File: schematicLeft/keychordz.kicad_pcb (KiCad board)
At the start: 2 copper layers, 124 x 101 mm, 45 parts, among them IC1 MCP73833-BZI_UN, J1 USB_C_Receptacle_USB2.0, J2 Conn_01x04_Male, J3 Conn_01x04_Male, SW1 SW_Push, SW2 SW_Push, SW3 SW_Push, SW4 SW_Push, SW5 SW_Push, SW6 SW_Push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

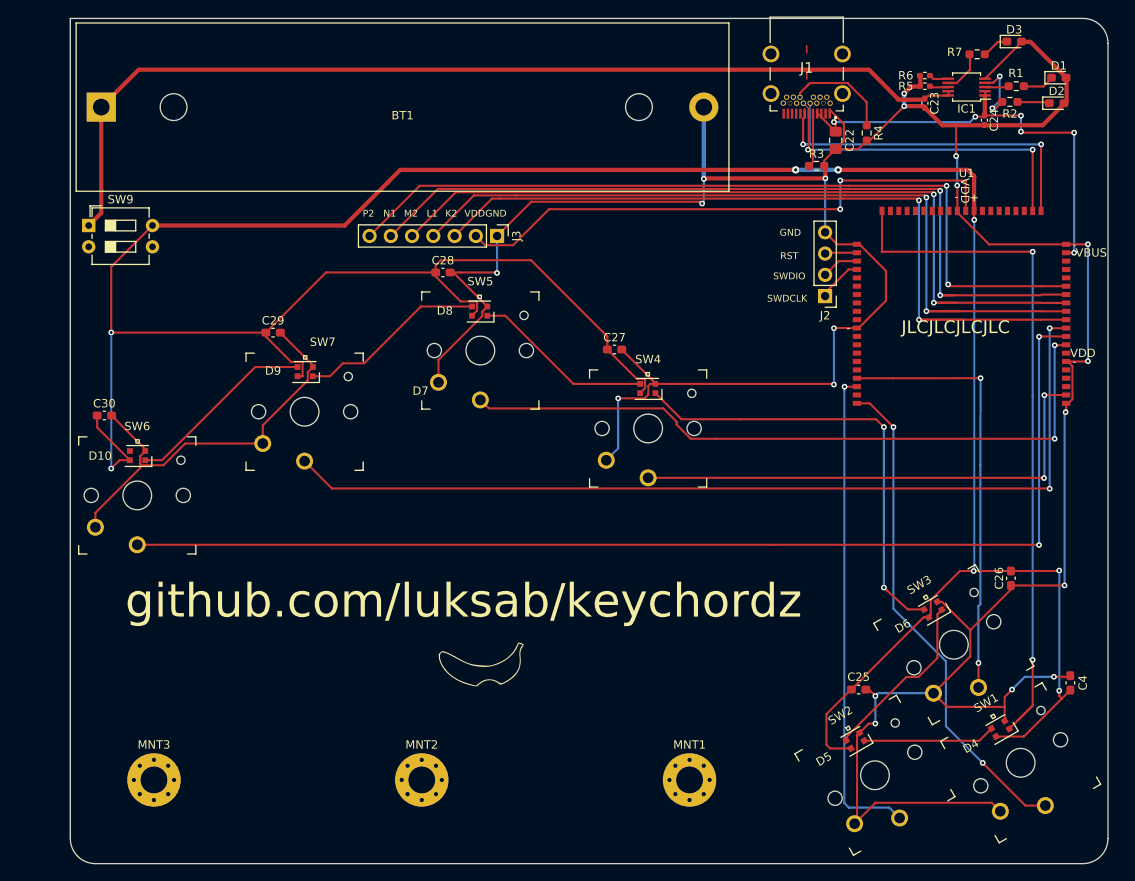
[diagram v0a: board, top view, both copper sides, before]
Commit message: change left PCB to STM32
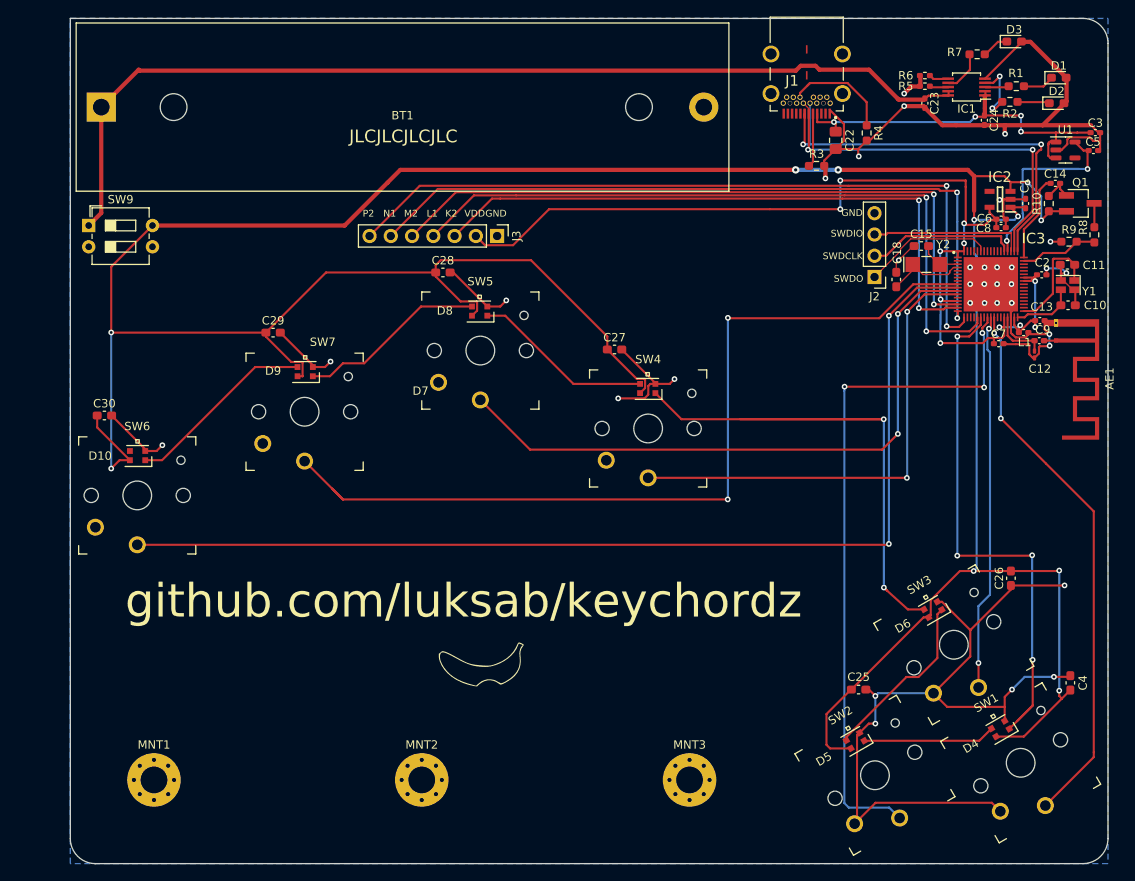
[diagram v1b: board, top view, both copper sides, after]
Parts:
- added AE1: PCB, RF_Antenna:Texas_SWRA117D_2.4GHz_Right, F.Cu at (129.8, 50.5)
- added C1: 1µF, Capacitor_SMD:C_0402_1005Metric_Pad0.74x0.62mm_HandSolder, F.Cu at (126.2, 34.1)
- added C10: 12pF, Capacitor_SMD:C_0603_1608Metric_Pad1.08x0.95mm_HandSolder, F.Cu at (131.2, 46.3)
- added C11: 12pF, Capacitor_SMD:C_0603_1608Metric_Pad1.08x0.95mm_HandSolder, F.Cu at (131.2, 41.4)
- added C12: 0.8pF, Capacitor_SMD:C_0201_0603Metric_Pad0.64x0.40mm_HandSolder, F.Cu at (127.2, 52.2)
- added C13: 1µF, Capacitor_SMD:C_0402_1005Metric_Pad0.74x0.62mm_HandSolder, F.Cu at (127.9, 48.1)
- added C14: 0.1µF, Capacitor_SMD:C_0402_1005Metric_Pad0.74x0.62mm_HandSolder, F.Cu at (129.7, 31.7)
- added C15: 12pF, Capacitor_SMD:C_0603_1608Metric_Pad1.08x0.95mm_HandSolder, F.Cu at (113.7, 39.2)
- added C18: 12pF, Capacitor_SMD:C_0603_1608Metric_Pad1.08x0.95mm_HandSolder, F.Cu at (110.7, 43.2)
- added C2: 1µF, Capacitor_SMD:C_0402_1005Metric_Pad0.74x0.62mm_HandSolder, F.Cu at (128.1, 42.6)
- added C3: 1µF, Capacitor_SMD:C_0402_1005Metric_Pad0.74x0.62mm_HandSolder, F.Cu at (134.5, 25.6)
- added C5: 1µF, Capacitor_SMD:C_0402_1005Metric_Pad0.74x0.62mm_HandSolder, F.Cu at (134.3, 27.8)
- added C6: 10µF, Capacitor_SMD:C_0402_1005Metric_Pad0.74x0.62mm_HandSolder, F.Cu at (123.2, 36.0)
- added C7: 1µF, Capacitor_SMD:C_0402_1005Metric_Pad0.74x0.62mm_HandSolder, F.Cu at (122.9, 50.9)
- added C8: 0.1µF, Capacitor_SMD:C_0402_1005Metric_Pad0.74x0.62mm_HandSolder, F.Cu at (123.2, 37.0)
- added C9: 100pF, Capacitor_SMD:C_0402_1005Metric_Pad0.74x0.62mm_HandSolder, F.Cu at (125.9, 49.5)
- added IC2: TPS7A2024PDBVR, SamacSys_Parts:SOT95P280X145-5N, F.Cu at (123.1, 33.6)
- added IC3: STM32WB55RGV7, SamacSys_Parts:QFN40P800X800X100-69N-D, F.Cu at (122.0, 43.8)
- added L1: 3.9nH, Inductor_SMD:L_0402_1005Metric_Pad0.77x0.64mm_HandSolder, F.Cu at (127.8, 50.5)
- added Q1: Q_PMOS_GSD, Package_TO_SOT_SMD:SC-59_Handsoldering, F.Cu at (132.7, 34.1)
- added R10: 10k, Resistor_SMD:R_0603_1608Metric_Pad0.98x0.95mm_HandSolder, F.Cu at (128.9, 34.1)
- added R8: 1k, Resistor_SMD:R_0603_1608Metric_Pad0.98x0.95mm_HandSolder, F.Cu at (134.4, 37.9)
- added R9: 1k, Resistor_SMD:R_0603_1608Metric_Pad0.98x0.95mm_HandSolder, F.Cu at (131.3, 38.7)
- added Y1: Crystal_GND23, Crystal:Crystal_SMD_2016-4Pin_2.0x1.6mm_HandSoldering, F.Cu at (131.2, 43.9)
- added Y2: Crystal, Crystal:Crystal_SMD_MicroCrystal_CC7V-T1A-2Pin_3.2x1.5mm_HandSoldering, F.Cu at (114.3, 41.4)
- J2: value Conn_01x04_Male -> DEBUG_CONN
- J3: value Conn_01x04_Male -> OLED_CONN
- U1: value nRF52840_Breakout -> MIC5504-3.3YM5; footprint schematic:nRF52840_Breakout -> Package_TO_SOT_SMD:SOT-23-5
- moved MNT1 64.0 mm to (22.0, 103.0)
- moved MNT3 64.0 mm to (86.0, 103.0)
- moved U1 14.0 mm to (130.9, 27.7)
- moved J2 6.33 mm to (108.1, 42.9)
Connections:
- D4 pad 2: Net-(D4-Pad2) -> LED_IN
- J2 pad 1: SWDCLK -> SWO
- J2 pad 2: SWDIO -> SWCLK
- J2 pad 3: RST -> SWDIO
- J3 pad 2: Net-(J3-Pad2) -> 2.4V
- J3 pad 3: Net-(J3-Pad3) -> SCK
- J3 pad 4: Net-(J3-Pad4) -> MOSI
- J3 pad 5: Net-(J3-Pad5) -> OLED_RES
- J3 pad 6: Net-(J3-Pad6) -> OLED_DC
- J3 pad 7: Net-(J3-Pad7) -> OLED_CS
- SW1 pad 1: Net-(SW1-Pad1) -> BTN1
- SW2 pad 1: Net-(SW2-Pad1) -> BTN2
- SW3 pad 1: Net-(SW3-Pad1) -> BTN3
- SW4 pad 1: Net-(SW4-Pad1) -> BTN4
- SW5 pad 1: Net-(SW5-Pad1) -> BTN5
- SW6 pad 1: Net-(SW6-Pad1) -> BTN6
- SW7 pad 1: Net-(SW7-Pad1) -> BTN7
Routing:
- net GND: track 434.9 -> 256.2 mm, vias 19 -> 34
- net Net-(SW6-Pad1): track 135.9 -> 0.00 mm, vias 2 -> 0
- net 2.4V: track 0.00 -> 127.1 mm, vias 0 -> 11
- net BTN6: track 0.00 -> 126.8 mm, vias 0 -> 2
- net Net-(SW7-Pad1): track 111.6 -> 0.00 mm, vias 2 -> 0
- net BTN7: track 0.00 -> 105.2 mm, vias 0 -> 2
- net Net-(J3-Pad7): track 97.3 -> 0.00 mm, vias 2 -> 0
- net Net-(J3-Pad6): track 97.2 -> 0.00 mm, vias 2 -> 0
- net Net-(J3-Pad5): track 96.1 -> 0.00 mm, vias 2 -> 0
- net Net-(J3-Pad4): track 95.4 -> 0.00 mm, vias 2 -> 0
- net Net-(J3-Pad3): track 94.6 -> 0.00 mm, vias 2 -> 0
- net OLED_CS: track 0.00 -> 91.3 mm, vias 0 -> 2
- net OLED_DC: track 0.00 -> 86.1 mm, vias 0 -> 2
- net MOSI: track 0.00 -> 84.3 mm, vias 0 -> 2
- net Net-(D4-Pad2): track 83.8 -> 0.00 mm, vias 2 -> 0
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- added copper zone on B.Cu, net GND
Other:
- board text added: "SWDO"
- board text removed: "RST"

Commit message: change OLED voltage to V_BAT (ordered this commit)
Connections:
- J3 pad 2: 2.4V -> V_BAT
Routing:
- net 2.4V: track 127.1 -> 57.7 mm, vias 11 -> 9
- net V_BAT: track 377.8 -> 380.8 mm
- net GND: track 256.2 -> 254.8 mm

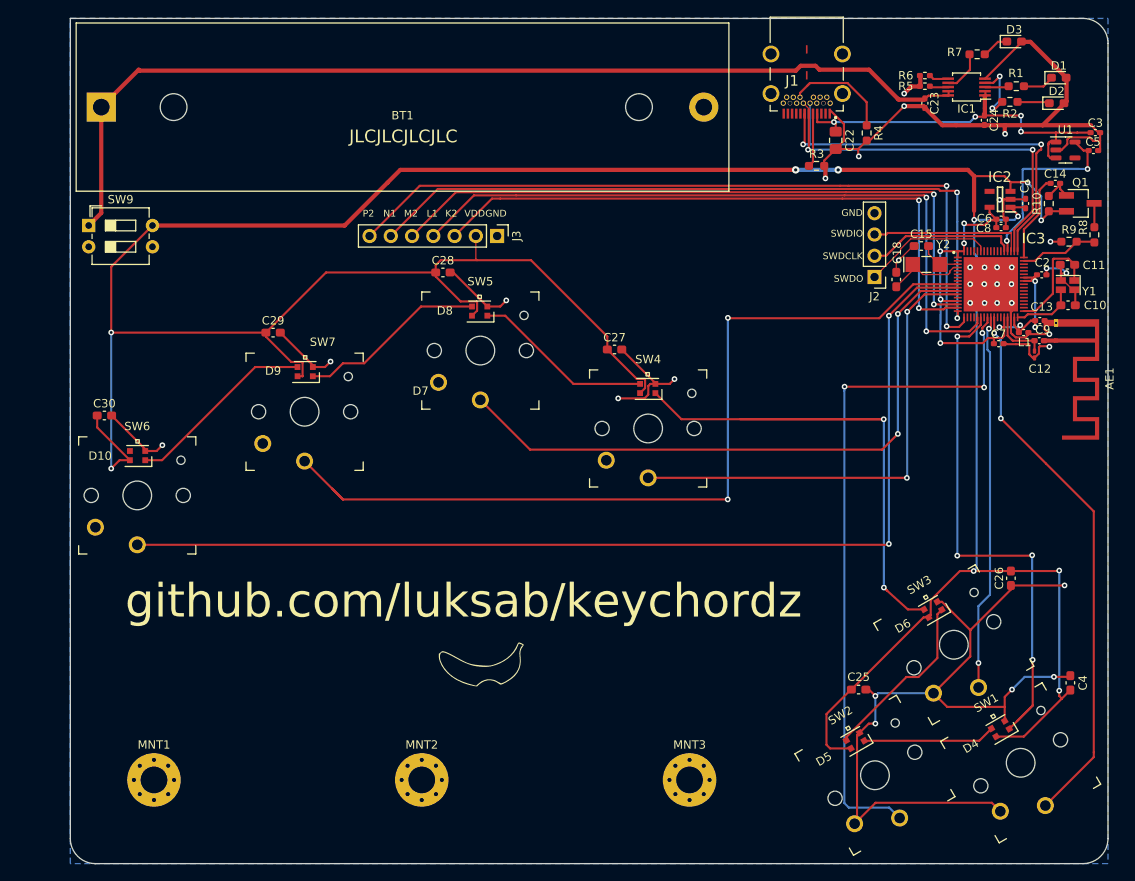
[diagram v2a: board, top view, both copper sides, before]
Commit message: use Arduino pro micro
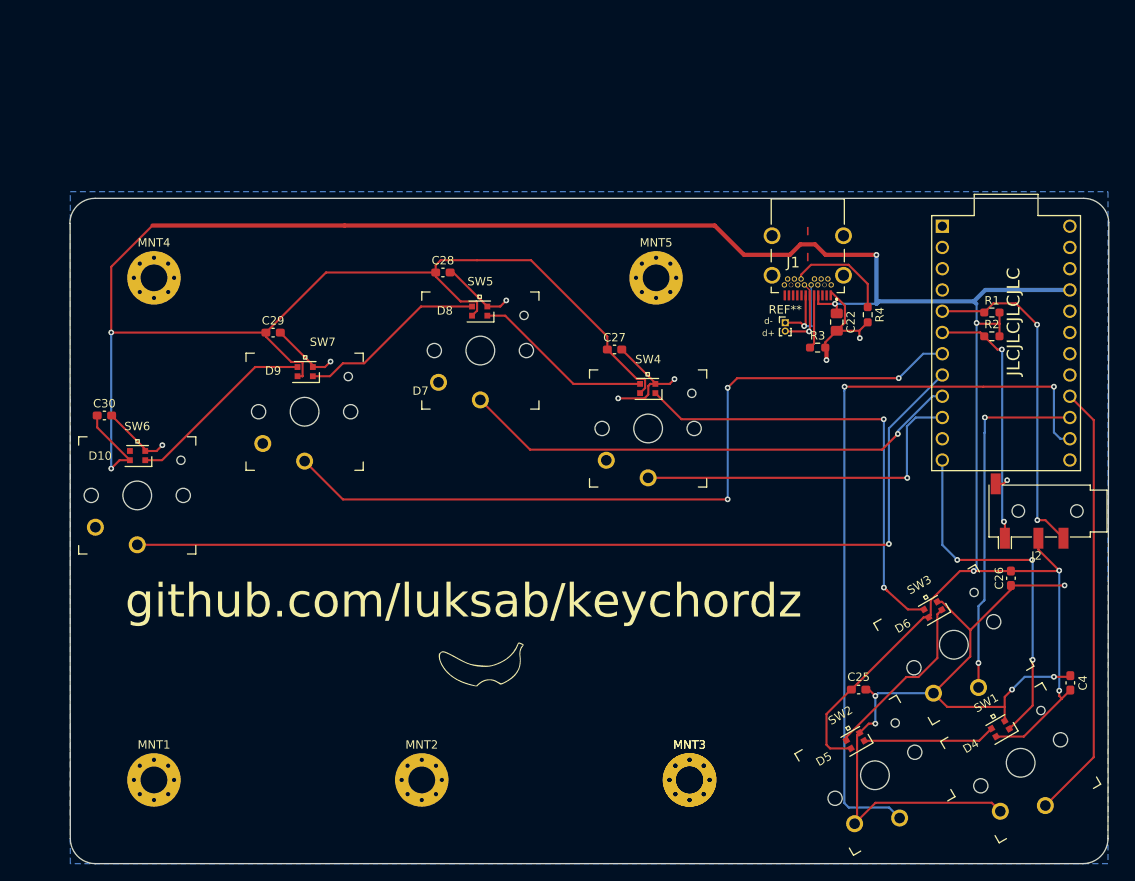
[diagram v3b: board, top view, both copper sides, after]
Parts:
- removed AE1: PCB, RF_Antenna:Texas_SWRA117D_2.4GHz_Right
- removed BT1: Battery_Cell, Battery:BatteryHolder_MPD_BH-18650-PC2
- removed C1, C13, C2, C23, C24, C3, C5, C7: 1µF, Capacitor_SMD:C_0402_1005Metric_Pad0.74x0.62mm_HandSolder
- removed C10, C11, C15, C18: 12pF, Capacitor_SMD:C_0603_1608Metric_Pad1.08x0.95mm_HandSolder
- removed C12: 0.8pF, Capacitor_SMD:C_0201_0603Metric_Pad0.64x0.40mm_HandSolder
- removed C14, C8: 0.1µF, Capacitor_SMD:C_0402_1005Metric_Pad0.74x0.62mm_HandSolder
- removed C6: 10µF, Capacitor_SMD:C_0402_1005Metric_Pad0.74x0.62mm_HandSolder
- removed C9: 100pF, Capacitor_SMD:C_0402_1005Metric_Pad0.74x0.62mm_HandSolder
- removed D1, D2, D3: LED_Small, LED_SMD:LED_0603_1608Metric_Pad1.05x0.95mm_HandSolder
- removed IC1: MCP73833-BZI_UN, Package_SO:MSOP-10_3x3mm_P0.5mm
- removed IC2: TPS7A2024PDBVR, SamacSys_Parts:SOT95P280X145-5N
- removed IC3: STM32WB55RGV7, SamacSys_Parts:QFN40P800X800X100-69N-D
- removed J3: OLED_CONN, Connector_PinHeader_2.54mm:PinHeader_1x07_P2.54mm_Vertical
- removed L1: 3.9nH, Inductor_SMD:L_0402_1005Metric_Pad0.77x0.64mm_HandSolder
- removed Q1: Q_PMOS_GSD, Package_TO_SOT_SMD:SC-59_Handsoldering
- removed R10: 10k, Resistor_SMD:R_0603_1608Metric_Pad0.98x0.95mm_HandSolder
- removed R5: 10k, Resistor_SMD:R_0402_1005Metric_Pad0.72x0.64mm_HandSolder
- removed R6: 1k, Resistor_SMD:R_0402_1005Metric_Pad0.72x0.64mm_HandSolder
- removed R7: 470, Resistor_SMD:R_0603_1608Metric_Pad0.98x0.95mm_HandSolder
- removed R8, R9: 1k, Resistor_SMD:R_0603_1608Metric_Pad0.98x0.95mm_HandSolder
- removed SW9: SW_SPST, Button_Switch_THT:SW_DIP_SPSTx02_Slide_6.7x6.64mm_W7.62mm_P2.54mm_LowProfile
- removed U1: MIC5504-3.3YM5, Package_TO_SOT_SMD:SOT-23-5
- removed Y1: Crystal_GND23, Crystal:Crystal_SMD_2016-4Pin_2.0x1.6mm_HandSoldering
- removed Y2: Crystal, Crystal:Crystal_SMD_MicroCrystal_CC7V-T1A-2Pin_3.2x1.5mm_HandSoldering
- added MNT3: MountingHole_3.2mm_M3_Pad_Via, MountingHole:MountingHole_3.2mm_M3_Pad_Via, F.Cu at (86.0, 103.0)
- added MNT4: MountingHole_3.2mm_M3_Pad_Via, MountingHole:MountingHole_3.2mm_M3_Pad_Via, F.Cu at (22.0, 43.0)
- added MNT5: MountingHole_3.2mm_M3_Pad_Via, MountingHole:MountingHole_3.2mm_M3_Pad_Via, F.Cu at (82.0, 43.0)
- added REF**: PinHeader_1x02_P1.00mm_Vertical, Connector_PinHeader_1.00mm:PinHeader_1x02_P1.00mm_Vertical, F.Cu at (97.4, 48.4)
- added U2: ProMicro, promicro:ProMicro, F.Cu at (123.8, 50.8)
- J2: value DEBUG_CONN -> AudioPlug4; footprint Connector_PinHeader_2.54mm:PinHeader_1x04_P2.54mm_Vertical -> Connector_Audio:Jack_3.5mm_PJ320D_Horizontal
- R1, R2: value 470 -> R_Small
- moved J2 34.0 mm to (127.5, 70.9)
- moved R2 28.1 mm to (122.1, 50.0), turned to 0 degrees
- moved R1 27.2 mm to (122.1, 47.1)
- moved C22 21.7 mm to (103.6, 48.3)
- moved R3 21.7 mm to (101.3, 51.3)
- moved J1 21.7 mm to (100.1, 39.6)
- moved R4 21.7 mm to (107.3, 47.4)
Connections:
- C25 pad 1: V_BAT -> +5V
- C26 pad 1: V_BAT -> +5V
- C27 pad 1: V_BAT -> +5V
- C28 pad 1: V_BAT -> +5V
- C29 pad 1: V_BAT -> +5V
- C30 pad 1: V_BAT -> +5V
- C4 pad 1: V_BAT -> +5V
- D10 pad 1: V_BAT -> +5V
- D4 pad 1: V_BAT -> +5V
- D5 pad 1: V_BAT -> +5V
- D6 pad 1: V_BAT -> +5V
- D7 pad 1: V_BAT -> +5V
- D8 pad 1: V_BAT -> +5V
- D9 pad 1: V_BAT -> +5V
- R1 pad 1: Net-(D1-Pad1) -> +5V
- R1 pad 2: Net-(IC1-Pad3) -> SDA
- R2 pad 1: Net-(D2-Pad1) -> SCK
- R2 pad 2: Net-(IC1-Pad4) -> +5V
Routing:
- net V_BAT: track 380.8 -> 0.00 mm, vias 11 -> 0
- net +5V: track 44.8 -> 374.5 mm, vias 4 -> 8
- net V_BAT_SW: track 120.5 -> 0.00 mm
- net GND: track 254.8 -> 149.3 mm, vias 34 -> 13
- net OLED_CS: track 91.3 -> 0.00 mm, vias 2 -> 0
- net OLED_DC: track 86.1 -> 0.00 mm, vias 2 -> 0
- net MOSI: track 84.3 -> 0.00 mm, vias 2 -> 0
- net OLED_RES: track 80.6 -> 0.00 mm, vias 2 -> 0
- net 2.4V: track 57.7 -> 0.00 mm, vias 9 -> 0
- net SCK: track 75.1 -> 30.7 mm
- net SDA: track 0.00 -> 40.3 mm, vias 0 -> 2
- net USB_D-: track 52.1 -> 12.0 mm, vias 2 -> 1
- net USB_D+: track 46.2 -> 9.19 mm, vias 2 -> 1
- net 3.3V_USB: track 29.4 -> 0.00 mm, vias 2 -> 0
- net LED_IN: track 64.0 -> 43.0 mm, vias 4 -> 3
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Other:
- board size 124 x 101 mm -> 124.1 x 79.5 mm
- board text added: "d+"
- board text added: "d-"
- board text removed: "GND"
- board text removed: "K2"
- board text removed: "L1"
- board text removed: "M2"
- board text removed: "N1"
- board text removed: "P2"
- board text removed: "SWDCLK"
- board text removed: "SWDIO"
- board text removed: "SWDO"
- board text removed: "VDD"

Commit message: fix LED vcc
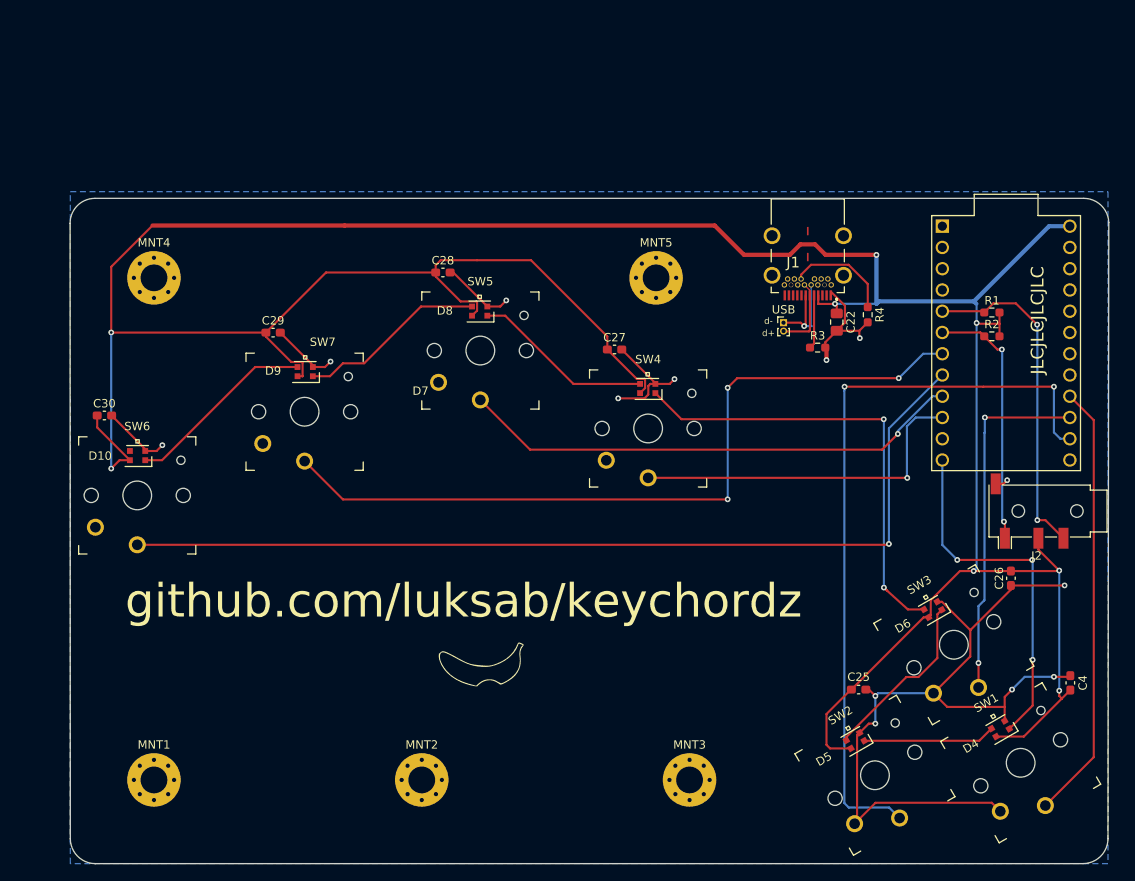
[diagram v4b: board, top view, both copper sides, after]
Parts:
- removed the MNT3 at (86.0, 103.0)
- removed REF**: PinHeader_1x02_P1.00mm_Vertical, Connector_PinHeader_1.00mm:PinHeader_1x02_P1.00mm_Vertical
- added USB: PinHeader_1x02_P1.00mm_Vertical, Connector_PinHeader_1.00mm:PinHeader_1x02_P1.00mm_Vertical, F.Cu at (97.2, 48.4)
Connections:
- U2 pad 21: +5V -> unconnected-(U2-Pad21)
- U2 pad 24: unconnected-(U2-Pad24) -> +5V
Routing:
- net +5V: track 374.5 -> 377.7 mm
- net USB_D+: vias 1 -> 0
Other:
- outline, holes or cut-outs redrawn
